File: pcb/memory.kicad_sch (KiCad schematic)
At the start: 5 parts, among them U4 IS66WVE4M16EBLL-70BLI

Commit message: second pcb iteration
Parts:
- added C26, C31: 100 nF, Capacitor_SMD:C_0402_1005Metric, symbol Device:C
- added U6: IS62WV5128EBLL-45BLI, nileswan:BGA-36_6x8_6.0x8.0mm, symbol nileswan:IS62WV5128EBLL-45BLI
- C21, C22, C23: footprint Capacitor_SMD:C_0603_1608Metric -> Capacitor_SMD:C_0402_1005Metric
- R23: footprint Resistor_SMD:R_0603_1608Metric -> Resistor_SMD:R_0402_1005Metric
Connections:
- net A0: now also U6.A1 (A0); no longer U4.A3 (A0)
- net A1: now also U4.A3 (A0), U6.A2 (A1); no longer U4.A4 (A1)
- net A10: now also U4.H3 (A9), U6.H2 (A10); no longer U4.H4 (A10)
- net A11: now also U4.H4 (A10), U6.H3 (A11); no longer U4.H5 (A11)
- net A12: now also U4.H5 (A11), U6.H4 (A12); no longer U4.G3 (A12)
- net A13: now also U4.G3 (A12), U6.H5 (A13); no longer U4.G4 (A13)
- net A14: now also U4.G4 (A13), U6.H6 (A14); no longer U4.F3 (A14)
- net A15: now also U4.F3 (A14), U6.G5 (A15); no longer U4.F4 (A15)
- net A2: now also U4.A4 (A1), U6.B2 (A2); no longer U4.A5 (A2)
- net A3: now also U4.A5 (A2), U6.A4 (A3); no longer U4.B3 (A3)
- net A4: now also U4.B3 (A3), U6.B4 (A4); no longer U4.B4 (A4)
- net A5: now also U4.B4 (A4), U6.C4 (A5); no longer U4.C3 (A5)
- net A6: now also U4.C3 (A5), U6.A5 (A6); no longer U4.C4 (A6)
- net A7: now also U4.C4 (A6), U6.B5 (A7); no longer U4.D4 (A7)
- net A8: now also U4.D4 (A7), U6.A6 (A8); no longer U4.H2 (A8)
- net A9: now also U4.H2 (A8), U6.H1 (A9); no longer U4.H3 (A9)
- net A_HIGH0: now also U4.F4 (A15), U6.G4 (A16); no longer U4.E4 (A16)
- net A_HIGH1: now also U4.E4 (A16), U6.F4 (A17); no longer U4.D3 (A17)
- net A_HIGH2: now also U4.D3 (A17), U6.F3 (A18); no longer U4.H1 (A18)
- net A_HIGH3: now also U4.H1 (A18); no longer U4.G2 (A19)
- net A_HIGH4: now also U4.G2 (A19); no longer U4.H6 (A20)
- net A_HIGH5: now also U4.H6 (A20); no longer U4.E3 (A21)
- net D0: now also U6.B6 (IO0)
- net D1: now also U6.C6 (IO1)
- net D2: now also U6.F6 (IO2)
- net D3: now also U6.G6 (IO3)
- net D4: now also U6.B1 (IO4)
- net D5: now also U6.C1 (IO5)
- net D6: now also U6.F1 (IO6)
- net D7: now also U6.G1 (IO7)
- net GND: now also C26.1, C31.1, U6.D1 (GND), U6.E6 (GND)
- net /OE: now also U6.G2 (OE#)
- net /WE: now also U6.B3 (WE#)
- net ENABLE_OUT_PSRAM renamed /PSRAM_LB
- net /PSRAM_LB: no longer U4.B2 (UB#)
- new net 3.3V_SRAM: C26.2, C31.2, U6.D6 (Vdd), U6.E1 (Vdd)
- new net A_HIGH6: U4.E3 (A21)
- new net /PSRAM_UB: U4.B2 (UB#)
- new net /SEL_SRAM: U6.G3 (CS#)

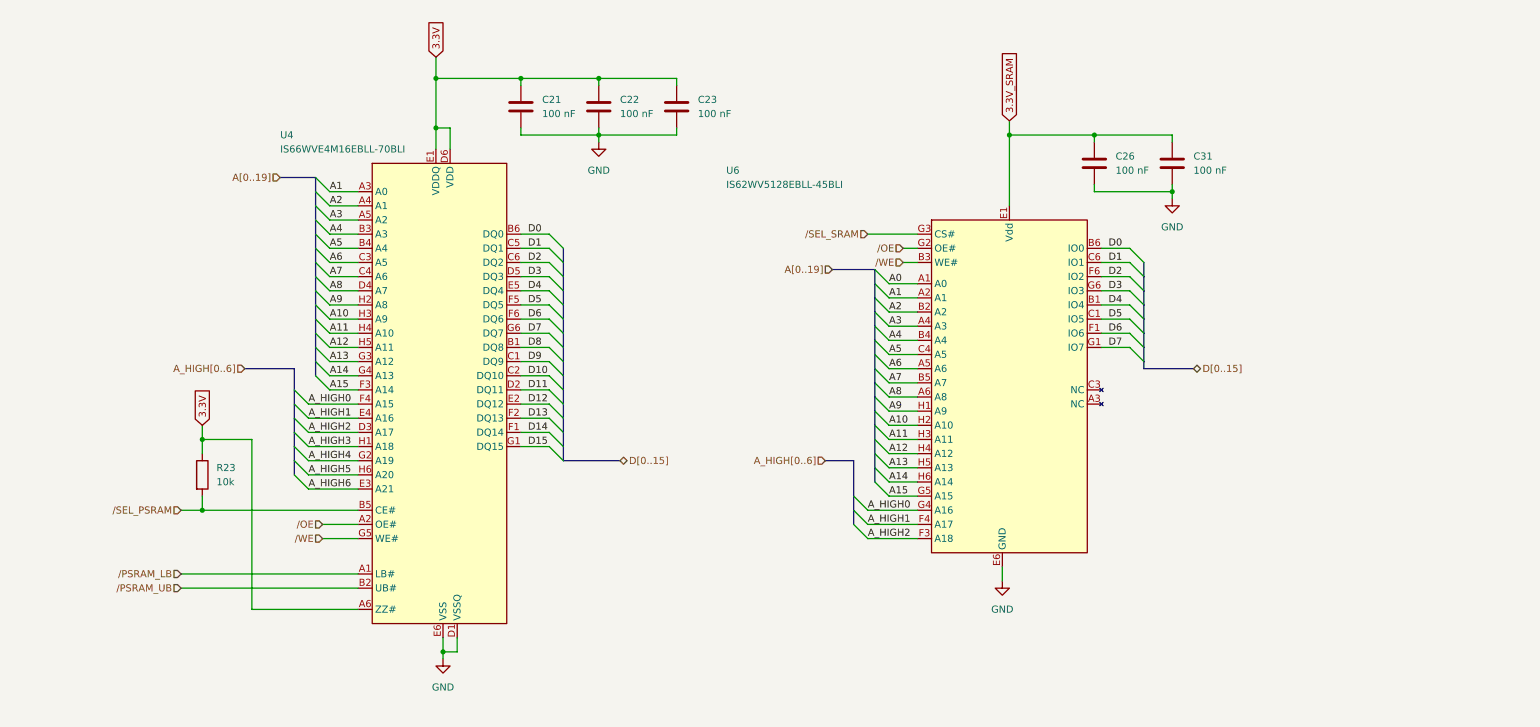
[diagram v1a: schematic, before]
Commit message: pcb revision 3 and 16 MB PSRAM support
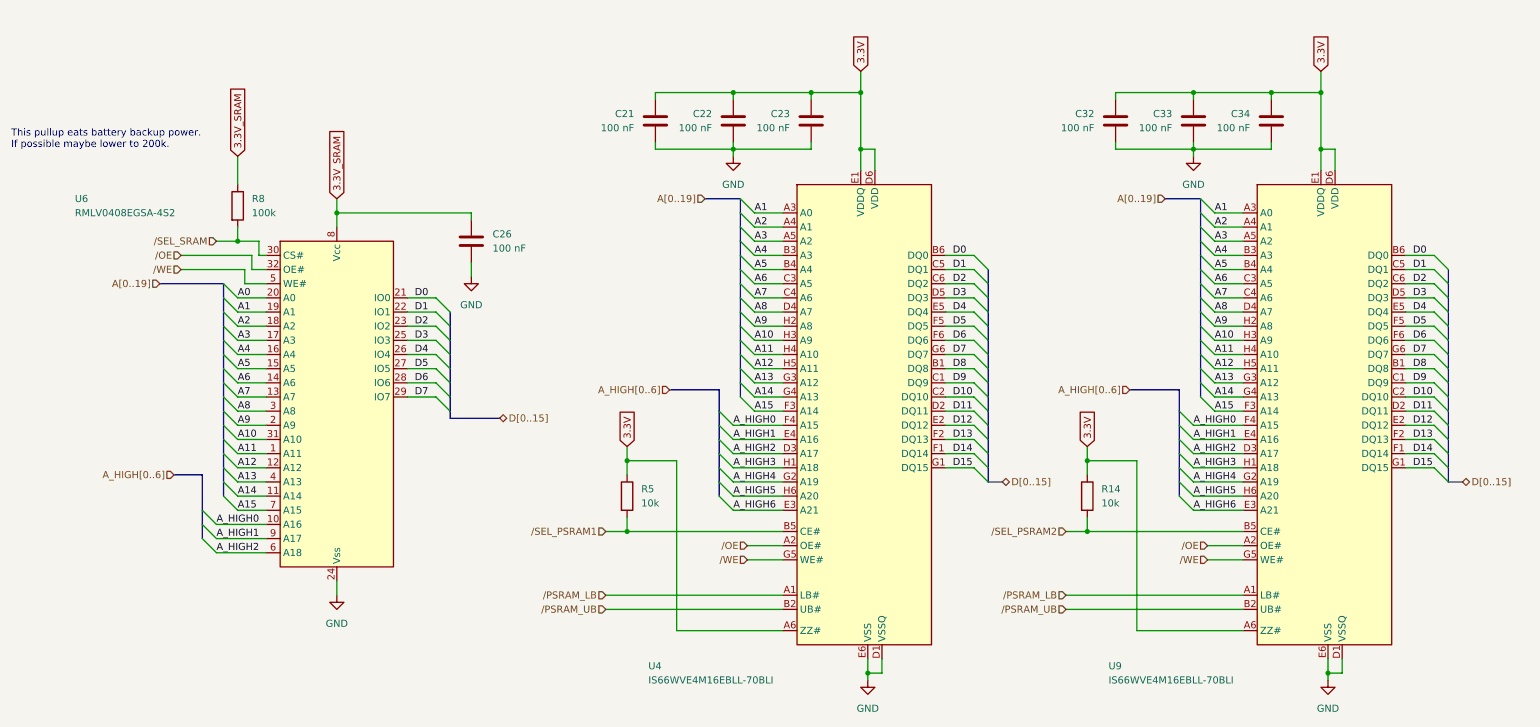
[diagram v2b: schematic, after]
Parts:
- removed C31: 100 nF, Capacitor_SMD:C_0402_1005Metric, symbol Device:C
- removed R23: 10k, Resistor_SMD:R_0402_1005Metric, symbol Device:R
- removed U6: IS62WV5128EBLL-45BLI, nileswan:BGA-36_6x8_6.0x8.0mm, symbol nileswan:IS62WV5128EBLL-45BLI
- added C32, C33, C34: 100 nF, Capacitor_SMD:C_0402_1005Metric, symbol Device:C
- added R14, R5: 10k, Resistor_SMD:R_0402_1005Metric, symbol Device:R
- added R8: 100k, Resistor_SMD:R_0402_1005Metric, symbol Device:R
- added U6: RMLV0408EGSA-4S2, nileswan:sTSOP-32, symbol nileswan:RMLV0408EGSA-4S2
- added U9: IS66WVE4M16EBLL-70BLI, nileswan:BGA-48_6x8_6.0x8.0mm, symbol nileswan:IS66WVE4M16EBLL-70BLI
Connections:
- net 3.3V: now also C32.2, C33.2, C34.2, R14.1, R5.1, U9.A6 (ZZ#), U9.D6 (VDD), U9.E1 (VDDQ)
- net 3.3V_SRAM: now also R8.1, U6.8 (Vcc)
- net A0: now also U6.20 (A0)
- net A1: now also U6.19 (A1), U9.A3 (A0)
- net A10: now also U6.31 (A10), U9.H3 (A9)
- net A11: now also U6.1 (A11), U9.H4 (A10)
- net A12: now also U6.12 (A12), U9.H5 (A11)
- net A13: now also U6.4 (A13), U9.G3 (A12)
- net A14: now also U6.11 (A14), U9.G4 (A13)
- net A15: now also U6.7 (A15), U9.F3 (A14)
- net A2: now also U6.18 (A2), U9.A4 (A1)
- net A3: now also U6.17 (A3), U9.A5 (A2)
- net A4: now also U6.16 (A4), U9.B3 (A3)
- net A5: now also U6.15 (A5), U9.B4 (A4)
- net A6: now also U6.14 (A6), U9.C3 (A5)
- net A7: now also U6.13 (A7), U9.C4 (A6)
- net A8: now also U6.3 (A8), U9.D4 (A7)
- net A9: now also U6.2 (A9), U9.H2 (A8)
- net A_HIGH0: now also U6.10 (A16), U9.F4 (A15)
- net A_HIGH1: now also U6.9 (A17), U9.E4 (A16)
- net A_HIGH2: now also U6.6 (A18), U9.D3 (A17)
- net A_HIGH3: now also U9.H1 (A18)
- net A_HIGH4: now also U9.G2 (A19)
- net A_HIGH5: now also U9.H6 (A20)
- net A_HIGH6: now also U9.E3 (A21)
- net D0: now also U6.21 (IO0), U9.B6 (DQ0)
- net D1: now also U6.22 (IO1), U9.C5 (DQ1)
- net D10: now also U9.C2 (DQ10)
- net D11: now also U9.D2 (DQ11)
- net D12: now also U9.E2 (DQ12)
- net D13: now also U9.F2 (DQ13)
- net D14: now also U9.F1 (DQ14)
- net D15: now also U9.G1 (DQ15)
- net D2: now also U6.23 (IO2), U9.C6 (DQ2)
- net D3: now also U6.25 (IO3), U9.D5 (DQ3)
- net D4: now also U6.26 (IO4), U9.E5 (DQ4)
- net D5: now also U6.27 (IO5), U9.F5 (DQ5)
- net D6: now also U6.28 (IO6), U9.F6 (DQ6)
- net D7: now also U6.29 (IO7), U9.G6 (DQ7)
- net D8: now also U9.B1 (DQ8)
- net D9: now also U9.C1 (DQ9)
- net GND: now also C32.1, C33.1, C34.1, U6.24 (Vss), U9.D1 (VSSQ), U9.E6 (VSS)
- net /OE: now also U6.32 (OE#), U9.A2 (OE#)
- net /PSRAM_LB: now also U9.A1 (LB#)
- net /PSRAM_UB: now also U9.B2 (UB#)
- net /SEL_SRAM: now also R8.2, U6.30 (CS#)
- net /WE: now also U6.5 (WE#), U9.G5 (WE#)
- net /SEL_PSRAM renamed /SEL_PSRAM1
- net /SEL_PSRAM1: now also R5.2
- new net /SEL_PSRAM2: R14.2, U9.B5 (CE#)
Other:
- note added: "This pullup eats battery backup power. If possible maybe lower to 200k."
- moved on the sheet: C26
